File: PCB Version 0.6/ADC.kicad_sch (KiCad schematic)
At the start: 4 parts, among them U9 TLV9002S_RUG_X2QFN

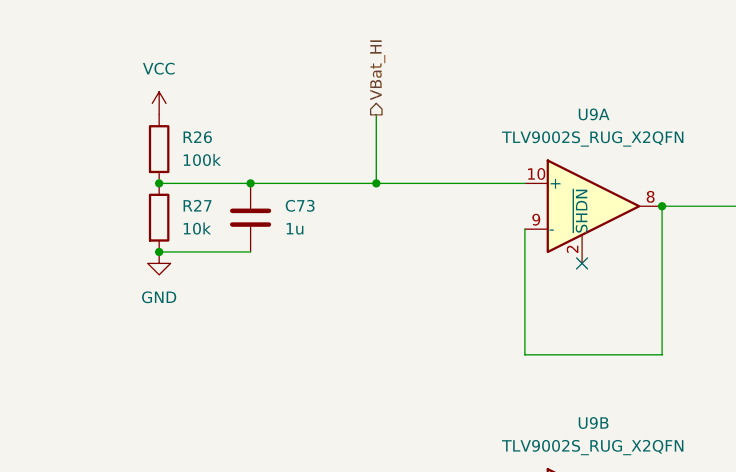
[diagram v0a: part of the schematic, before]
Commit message: replace USB JST with pads and remove USB TVS
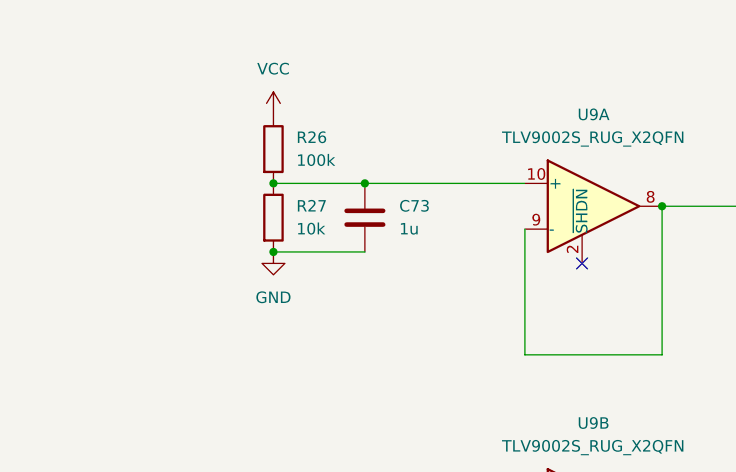
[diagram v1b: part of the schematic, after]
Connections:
- net VBat_HI: no longer names the net of C73.2, R26.2, R27.1, U9.10 (+)
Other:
- moved on the sheet: C73, R26, R27
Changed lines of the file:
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@@
 	)
 	(junction
-		(at 60.96 43.18)
+		(at 73.66 43.18)
 		(diameter 0)
 		(color 0 0 0 0)
 	)
 	(junction
-		(at 71.12 35.56)
+		(at 83.82 35.56)
 		(diameter 0)
 		(color 0 0 0 0)
@@
 	)
 	(junction
-		(at 60.96 35.56)
+		(at 73.66 35.56)
 		(diameter 0)
 		(color 0 0 0 0)
@@
 		(color 0 0 0 0)
 	)
-	(junction
-		(at 85.09 35.56)
-		(diameter 0)
-		(color 0 0 0 0)
-	)
 	(no_connect
 		(at 107.95 44.45)
@@
 	(wire
 		(pts
-			(xy 60.96 35.56) (xy 71.12 35.56)
+			(xy 73.66 35.56) (xy 83.82 35.56)
 		)
 		(stroke
@@
 	(wire
 		(pts
-			(xy 71.12 35.56) (xy 85.09 35.56)
-		)
-		(stroke
-			(width 0)
-			(type default)
-		)
-	)
-	(wire
-		(pts
-			(xy 85.09 27.94) (xy 85.09 35.56)
-		)
-		(stroke
-			(width 0)
-			(type default)
-		)
-	)
-	(wire
-		(pts
 			(xy 116.84 54.61) (xy 116.84 38.1)
 		)
@@
 	(wire
 		(pts
-			(xy 85.09 35.56) (xy 101.6 35.56)
+			(xy 83.82 35.56) (xy 101.6 35.56)
 		)
 		(stroke
@@
 	(wire
 		(pts
-			(xy 60.96 43.18) (xy 71.12 43.18)
+			(xy 73.66 43.18) (xy 83.82 43.18)
 		)
 		(stroke
@@
 		(shape output)
 		(at 168.91 59.69 0)
-		(effects
-			(font
-				(size 1.27 1.27)
-			)
-			(justify left)
-		)
-	)
-	(hierarchical_label "VBat_HI"
-		(shape output)
-		(at 85.09 27.94 90)
 		(effects
 			(font
@@
 	(symbol
 		(lib_id "power:VCC")
-		(at 60.96 27.94 0)
+		(at 73.66 27.94 0)
 		(unit 1)
 		(exclude_from_sim no)
@@
 		(fields_autoplaced yes)
 		(property "Reference" "#PWR150"
-			(at 60.96 31.75 0)
+			(at 73.66 31.75 0)
 			(effects
 				(font
@@
 		)
 		(property "Value" "VCC"
-			(at 60.96 22.86 0)
+			(at 73.66 22.86 0)
 			(effects
 				(font
@@
 		)
 		(property "Footprint" ""
-			(at 60.96 27.94 0)
+			(at 73.66 27.94 0)
 			(effects
 				(font
@@
 		)
 		(property "Datasheet" ""
-			(at 60.96 27.94 0)
+			(at 73.66 27.94 0)
 			(effects
 				(font
@@
 		)
 		(property "Description" "Power symbol creates a global label with name \"VCC\""
-			(at 60.96 27.94 0)
+			(at 73.66 27.94 0)
 			(effects
 				(font
@@
 	(symbol
 		(lib_id "Device:C")
-		(at 71.12 39.37 180)
+		(at 83.82 39.37 180)
 		(unit 1)
 		(exclude_from_sim no)
@@
 		(fields_autoplaced yes)
 		(property "Reference" "C73"
-			(at 74.93 38.0999 0)
+			(at 87.63 38.0999 0)
 			(effects
 				(font
@@
 		)
 		(property "Value" "1u"
-			(at 74.93 40.6399 0)
+			(at 87.63 40.6399 0)
 			(effects
 				(font
@@
 		)
 		(property "Footprint" "Capacitor_SMD:C_0402_1005Metric"
-			(at 70.1548 35.56 0)
+			(at 82.8548 35.56 0)
 			(effects
 				(font
@@
 		)
 		(property "Datasheet" "~"
-			(at 71.12 39.37 0)
+			(at 83.82 39.37 0)
 			(effects
 				(font
@@
 		)
 		(property "Description" "Unpolarized capacitor"
-			(at 71.12 39.37 0)
+			(at 83.82 39.37 0)
 			(effects
 				(font
@@
 	(symbol
 		(lib_id "power:GND")
-		(at 60.96 43.18 0)
+		(at 73.66 43.18 0)
 		(unit 1)
 		(exclude_from_sim no)
@@
 		(fields_autoplaced yes)
 		(property "Reference" "#PWR151"
-			(at 60.96 49.53 0)
+			(at 73.66 49.53 0)
 			(effects
 				(font
@@
 		)
 		(property "Value" "GND"
-			(at 60.96 48.26 0)
+			(at 73.66 48.26 0)
 			(effects
 				(font
@@
 		)
 		(property "Footprint" ""
-			(at 60.96 43.18 0)
+			(at 73.66 43.18 0)
 			(effects
 				(font
@@
 		)
 		(property "Datasheet" ""
-			(at 60.96 43.18 0)
+			(at 73.66 43.18 0)
 			(effects
 				(font
@@
 		)
 		(property "Description" "Power symbol creates a global label with name \"GND\" , ground"
-			(at 60.96 43.18 0)
+			(at 73.66 43.18 0)
 			(effects
 				(font
@@
 	(symbol
 		(lib_id "Device:R")
-		(at 60.96 31.75 0)
+		(at 73.66 31.75 0)
 		(unit 1)
 		(exclude_from_sim no)
@@
 		(fields_autoplaced yes)
 		(property "Reference" "R26"
-			(at 63.5 30.4799 0)
+			(at 76.2 30.4799 0)
 			(effects
 				(font
@@
 		)
 		(property "Value" "100k"
-			(at 63.5 33.0199 0)
+			(at 76.2 33.0199 0)
 			(effects
 				(font
@@
 		)
 		(property "Footprint" "Resistor_SMD:R_0402_1005Metric"
-			(at 59.182 31.75 90)
+			(at 71.882 31.75 90)
 			(effects
 				(font
@@
 		)
 		(property "Datasheet" "~"
-			(at 60.96 31.75 0)
+			(at 73.66 31.75 0)
 			(effects
 				(font
@@
 		)
 		(property "Description" "Resistor"
-			(at 60.96 31.75 0)
+			(at 73.66 31.75 0)
 			(effects
 				(font
@@
 	(symbol
 		(lib_id "Device:R")
-		(at 60.96 39.37 0)
+		(at 73.66 39.37 0)
 		(unit 1)
 		(exclude_from_sim no)
@@
 		(fields_autoplaced yes)
 		(property "Reference" "R27"
-			(at 63.5 38.0999 0)
+			(at 76.2 38.0999 0)
 			(effects
 				(font
@@
 		)
 		(property "Value" "10k"
-			(at 63.5 40.6399 0)
+			(at 76.2 40.6399 0)
 			(effects
 				(font
@@
 		)
 		(property "Footprint" "Resistor_SMD:R_0402_1005Metric"
-			(at 59.182 39.37 90)
+			(at 71.882 39.37 90)
 			(effects
 				(font
@@
 		)
 		(property "Datasheet" "~"
-			(at 60.96 39.37 0)
+			(at 73.66 39.37 0)
 			(effects
 				(font
@@
 		)
 		(property "Description" "Resistor"
-			(at 60.96 39.37 0)
-			(effects
-				(font
+			(at 73.66 39.37 0)
+			(effects
+				(font

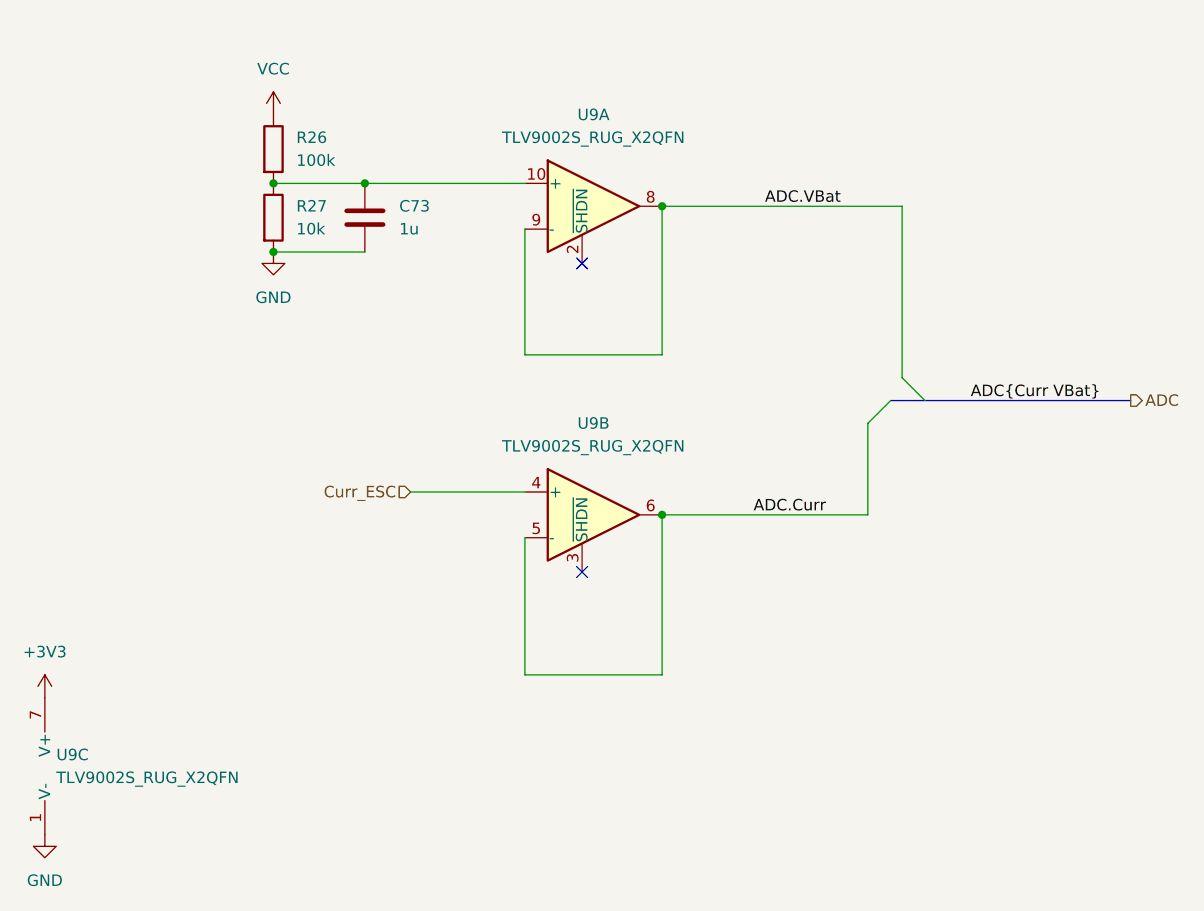
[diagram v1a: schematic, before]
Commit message: remove current sensor ADC, swap opamp, add dcdc switch
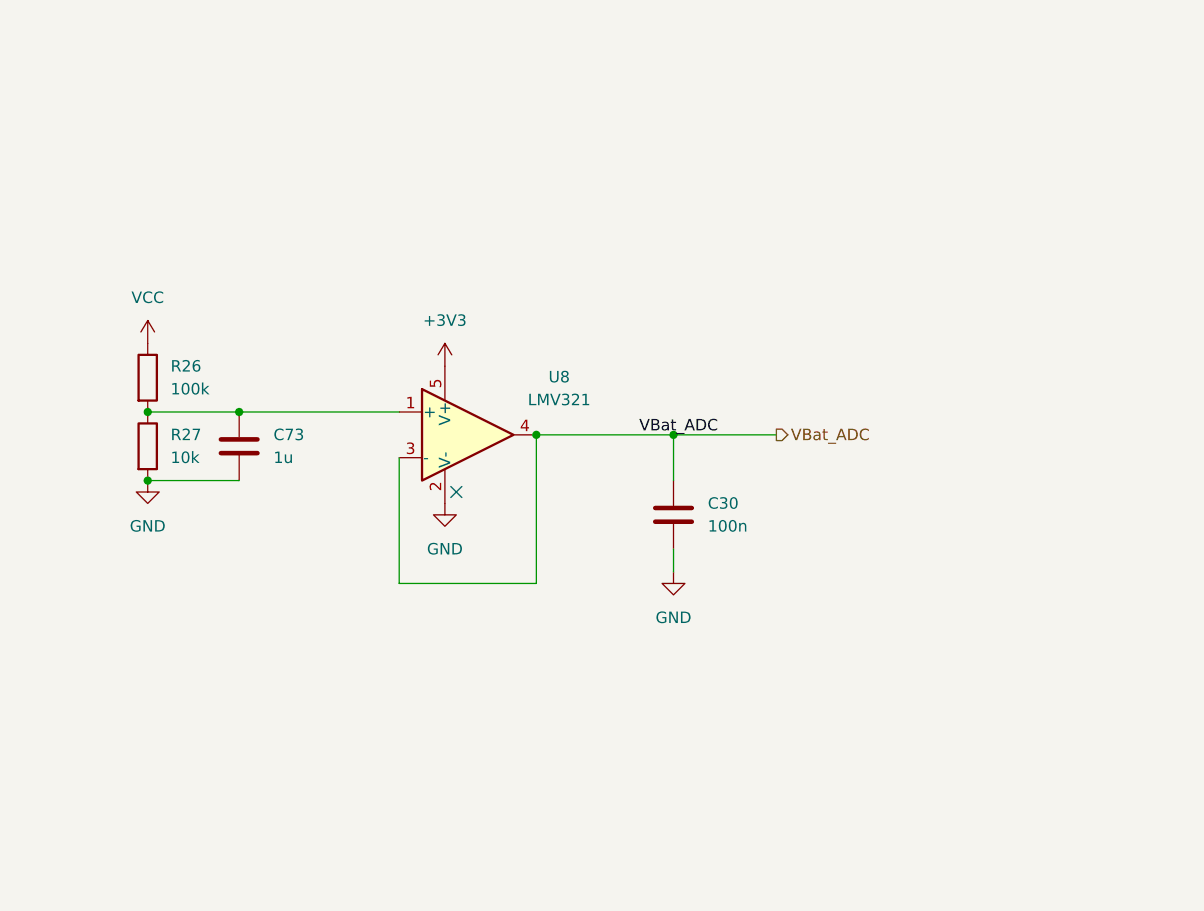
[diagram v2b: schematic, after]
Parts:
- removed U9: TLV9002S_RUG_X2QFN, Kolibri custom:Texas_X2QFN_RUG_10pin_1.5x2mm, symbol Kolibri custom:TLV9002S_RUG_X2QFN
- added C30: 100n, Capacitor_SMD:C_0402_1005Metric, symbol Device:C
- added U8: LMV321, Package_TO_SOT_SMD:SOT-353_SC-70-5, symbol Amplifier_Operational:LMV321
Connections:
- net +3V3: now also U8.5 (V+)
- net GND: now also C30.2, U8.2 (V-)
- net at C73.2, R26.2, R27.1: now also U8.1 (+)
- new net VBat_ADC: C30.1, U8.3 (-), U8.4
- no-connect marks 2 -> 1
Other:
- moved on the sheet: C73, R26, R27

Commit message: wip routing
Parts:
- U8: value LMV321 -> C3029047
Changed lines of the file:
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@@
 			)
 		)
-		(property "Value" "LMV321"
+		(property "Value" "C3029047"
 			(at 105.41 59.6198 0)
 			(effects
